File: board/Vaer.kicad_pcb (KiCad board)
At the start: 2 copper layers, 0 parts

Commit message: :sparkles: Add an initial outline for the board
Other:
- board outline added: 84.4 x 84.4 mm
- board text added: "${TITLE} Version ${REVISION} Design finished on ${ISSUE_DATE}"

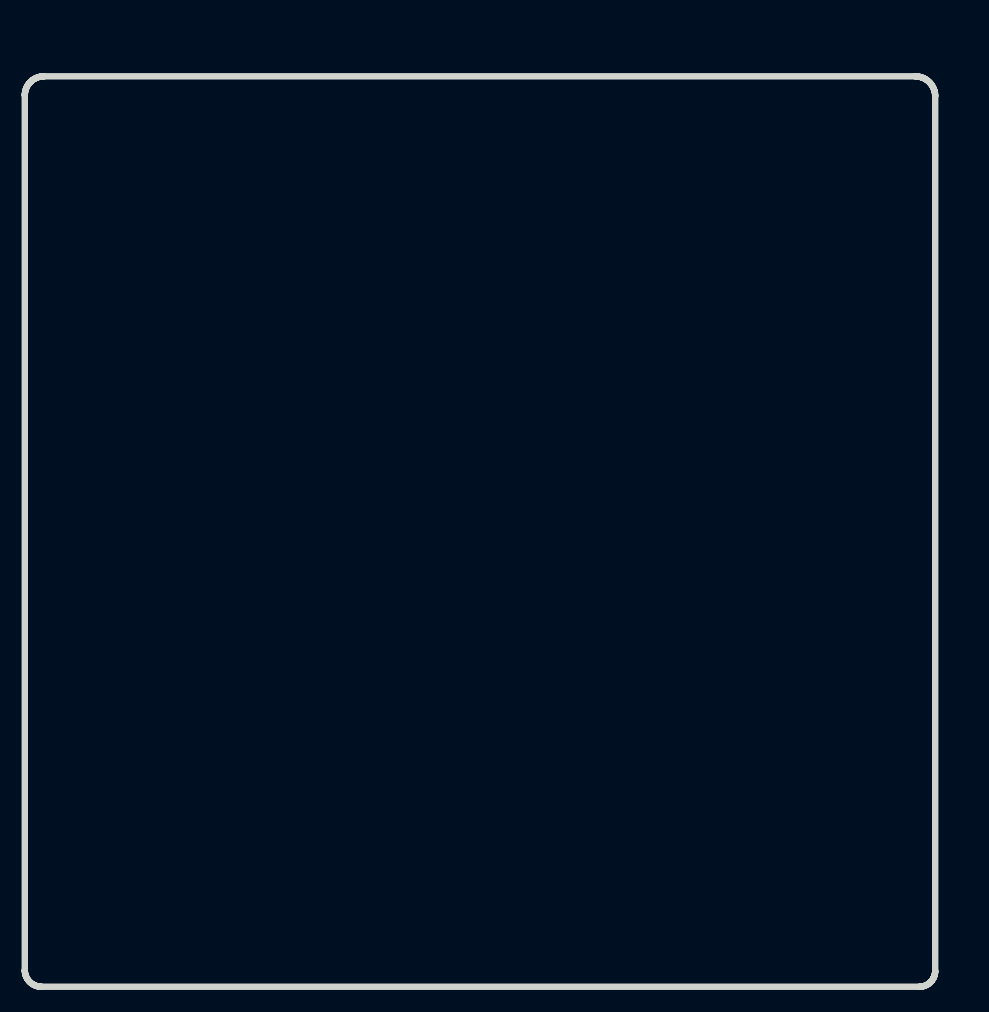
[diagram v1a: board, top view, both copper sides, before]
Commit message: :recycle: Add a notch for the PCB antenna of the MCU
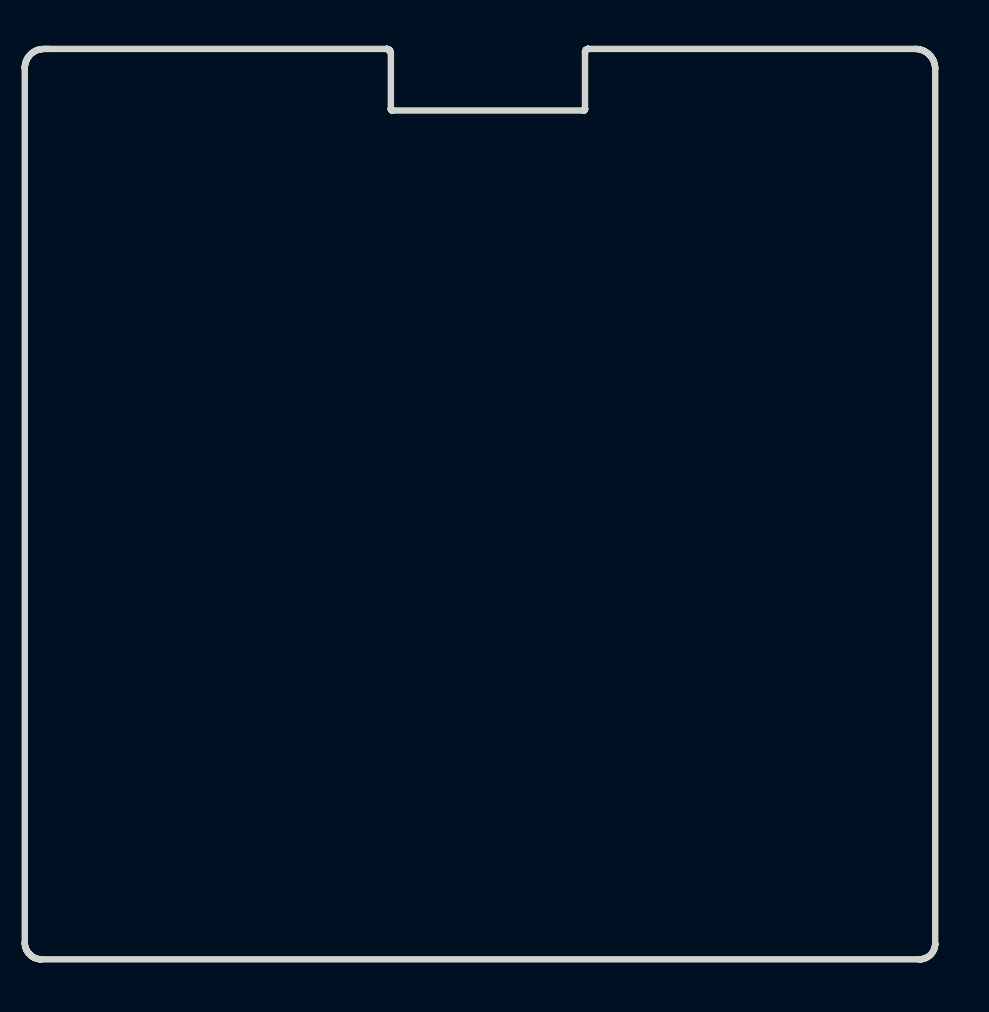
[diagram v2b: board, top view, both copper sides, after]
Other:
- outline, holes or cut-outs redrawn

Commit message: :construction: Start layouting the actual PCB
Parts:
- added BT1: Battery_Cell, Battery:BatteryHolder_MPD_BH-18650-PC2, F.Cu at (110.0, 111.8)
- added C1: 100nF, Capacitor_SMD:C_1206_3216Metric_Pad1.33x1.80mm_HandSolder, F.Cu at (110.4, 72.2)
- added C2: 100nF, Capacitor_SMD:C_1206_3216Metric_Pad1.33x1.80mm_HandSolder, F.Cu at (110.4, 77.3)
- added C3: 4.7uF, Capacitor_SMD:C_1206_3216Metric_Pad1.33x1.80mm_HandSolder, F.Cu at (133.0, 93.0)
- added C4: 10uF, Capacitor_SMD:C_1206_3216Metric_Pad1.33x1.80mm_HandSolder, F.Cu at (162.6, 86.4)
- added C5: 10uF, Capacitor_SMD:C_1206_3216Metric_Pad1.33x1.80mm_HandSolder, F.Cu at (167.6, 86.4)
- added C6: 1uF, Capacitor_SMD:C_1206_3216Metric_Pad1.33x1.80mm_HandSolder, F.Cu at (124.4, 93.0)
- added D1: LED_BLUE_PWR, LED_SMD:LED_1206_3216Metric_Pad1.42x1.75mm_HandSolder, F.Cu at (178.9, 76.2)
- added D2: LED_YELLOW, LED_SMD:LED_1206_3216Metric_Pad1.42x1.75mm_HandSolder, F.Cu at (178.9, 71.1)
- added D3: LED_GREEN, LED_SMD:LED_1206_3216Metric_Pad1.42x1.75mm_HandSolder, F.Cu at (178.9, 66.0)
- added H1: MountingHole_Pad, MountingHole:MountingHole_2.2mm_M2_Pad_Via, F.Cu at (108.0, 53.3)
- added H2: MountingHole_Pad, MountingHole:MountingHole_2.2mm_M2_Pad_Via, F.Cu at (184.5, 53.3)
- added H3: MountingHole_Pad, MountingHole:MountingHole_2.2mm_M2_Pad_Via, F.Cu at (108.0, 127.8)
- added H4: MountingHole_Pad, MountingHole:MountingHole_2.2mm_M2_Pad_Via, F.Cu at (184.5, 127.8)
- added J1: 105450-0101, Library:MOLEX_105450-0101, F.Cu at (138.5, 129.9)
- added R1: 5k1, Resistor_SMD:R_1206_3216Metric_Pad1.30x1.75mm_HandSolder, F.Cu at (152.5, 127.0)
- added R2: 5k1, Resistor_SMD:R_1206_3216Metric_Pad1.30x1.75mm_HandSolder, F.Cu at (152.5, 130.4)
- added R3: 120, Resistor_SMD:R_1206_3216Metric_Pad1.30x1.75mm_HandSolder, F.Cu at (168.8, 76.2)
- added R4: 1k5, Resistor_SMD:R_1206_3216Metric_Pad1.30x1.75mm_HandSolder, F.Cu at (168.8, 71.1)
- added R5: 1k5, Resistor_SMD:R_1206_3216Metric_Pad1.30x1.75mm_HandSolder, F.Cu at (168.8, 66.0)
- added R6: 10k, Resistor_SMD:R_1206_3216Metric_Pad1.30x1.75mm_HandSolder, F.Cu at (124.4, 97.1)
- added R7: 10k, Resistor_SMD:R_1206_3216Metric_Pad1.30x1.75mm_HandSolder, F.Cu at (142.2, 86.4)
- added R8: 1k18, Resistor_SMD:R_1206_3216Metric_Pad1.30x1.75mm_HandSolder, F.Cu at (147.3, 86.4)
- added R9: 1k13, Resistor_SMD:R_1206_3216Metric_Pad1.30x1.75mm_HandSolder, F.Cu at (152.4, 86.4)
- added SW_FLASH1: Flash mode, Button_Switch_THT:SW_PUSH_6mm, F.Cu at (177.1, 93.0)
- added SW_RESET1: Reset, Button_Switch_THT:SW_PUSH_6mm, F.Cu at (108.5, 93.0)
- added TP1: TestPoint, TestPoint:TestPoint_Pad_D1.0mm, F.Cu at (177.1, 88.9)
- added TP2: TestPoint, TestPoint:TestPoint_Pad_D1.0mm, F.Cu at (108.5, 88.9)
- added U2: NCP1117-3.3_SOT223, Package_TO_SOT_SMD:SOT-223-3_TabPin2, F.Cu at (165.1, 95.2)
- added U3: BQ24073RGT, Package_DFN_QFN:VQFN-16-1EP_3x3mm_P0.5mm_EP1.6x1.6mm, F.Cu at (146.6, 94.8)
- added U4: BME280, Package_LGA:Bosch_LGA-8_2.5x2.5mm_P0.65mm_ClockwisePinNumbering, F.Cu at (117.1, 74.7)
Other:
- board text added: "Humidity Pressure Temperature"
- board text added: "PWR"
- board text added: "TP EN"
- board text added: "TP PROG"
- board text added: "locked"
- board text added: "~{CHG}"
- board text added: "~{PGOOD}"
- board text removed: "${TITLE} Version ${REVISION} Design finished on ${ISSUE_DATE}"

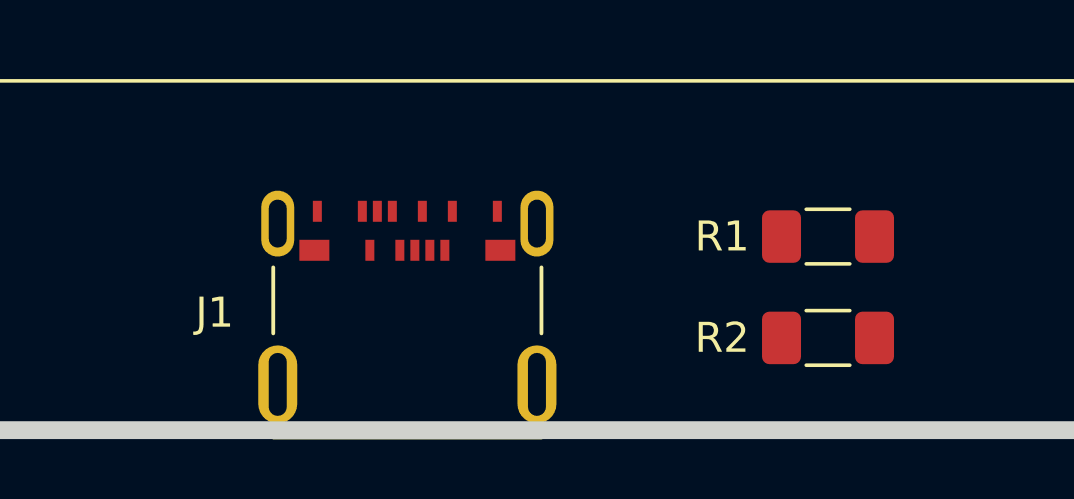
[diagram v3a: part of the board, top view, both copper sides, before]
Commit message: :fire: Remove dysfunctional libraries
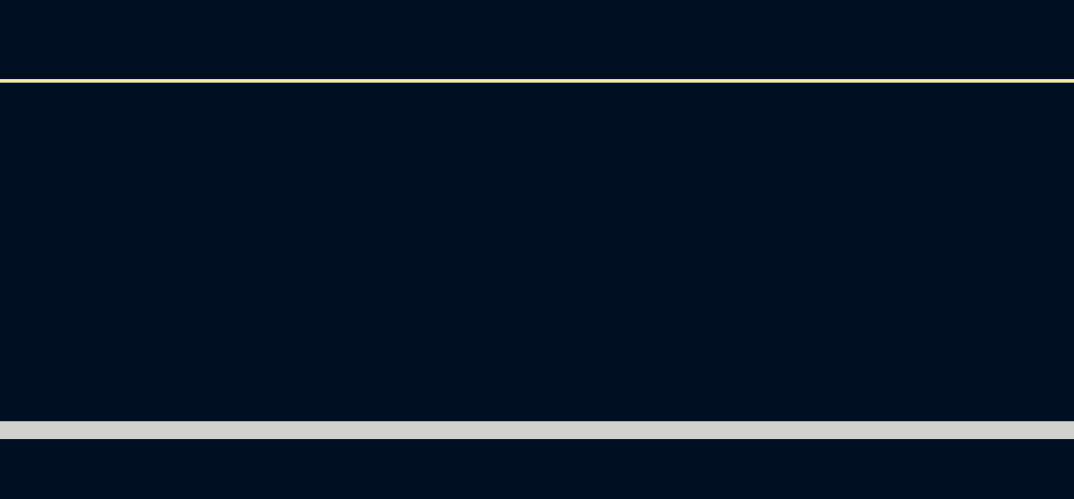
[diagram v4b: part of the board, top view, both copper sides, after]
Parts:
- removed J1: 105450-0101, Library:MOLEX_105450-0101
- removed R1, R2: 5k1, Resistor_SMD:R_1206_3216Metric_Pad1.30x1.75mm_HandSolder

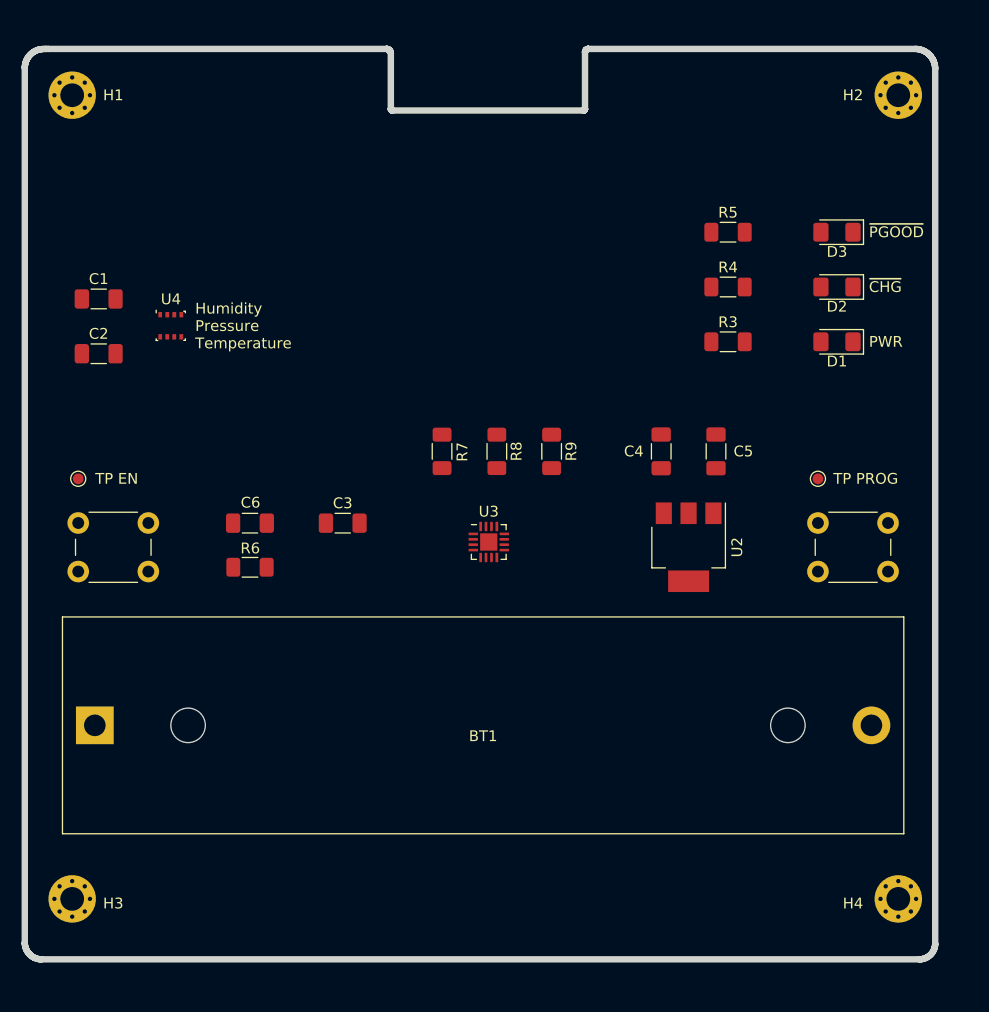
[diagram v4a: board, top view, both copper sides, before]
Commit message: :sparkles: Place all components onto the board
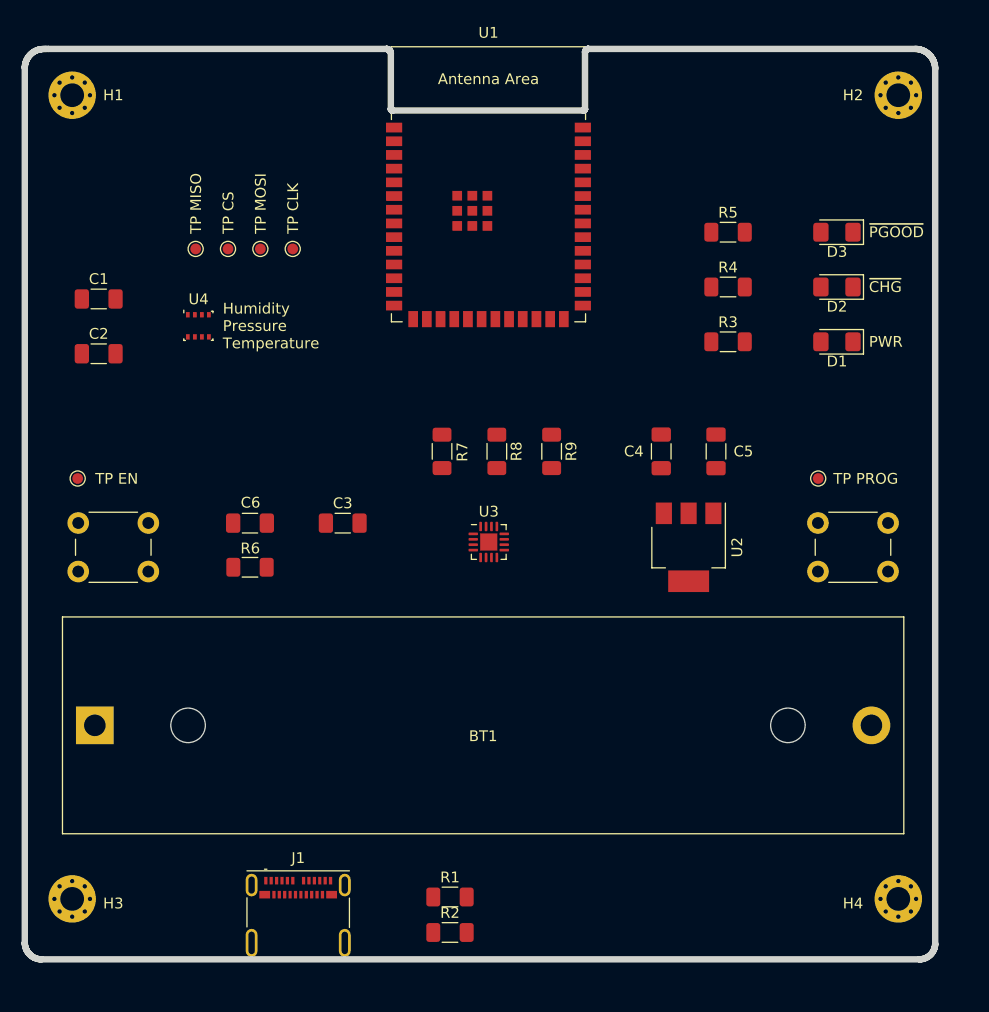
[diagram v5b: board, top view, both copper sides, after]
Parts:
- added J1: USB_C_Receptacle, Connector_USB:USB_C_Receptacle_Molex_105450-0101, F.Cu at (128.9, 129.4)
- added R1: 5k1, Resistor_SMD:R_1206_3216Metric_Pad1.30x1.75mm_HandSolder, F.Cu at (143.0, 127.7)
- added R2: 5k1, Resistor_SMD:R_1206_3216Metric_Pad1.30x1.75mm_HandSolder, F.Cu at (143.0, 131.0)
- added TP3: TestPoint, TestPoint:TestPoint_Pad_D1.0mm, F.Cu at (125.4, 67.6)
- added TP4: TestPoint, TestPoint:TestPoint_Pad_D1.0mm, F.Cu at (128.4, 67.6)
- added TP5: TestPoint, TestPoint:TestPoint_Pad_D1.0mm, F.Cu at (177.1, 88.9)
- added TP6: TestPoint, TestPoint:TestPoint_Pad_D1.0mm, F.Cu at (108.5, 88.9)
- added U1: ESP32-S3-WROOM-1, Espressif:ESP32-S3-WROOM-1, F.Cu at (146.5, 64.6)
- moved TP1 61.5 mm to (119.4, 67.6)
- moved TP2 25.4 mm to (122.4, 67.6)
- moved U4 2.56 mm to (119.6, 74.7)
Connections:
- TP1 pad 1: PROG -> MISO
- TP2 pad 1: EN -> CS
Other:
- board text added: "TP CLK"
- board text added: "TP CS"
- board text added: "TP MISO"
- board text added: "TP MOSI"

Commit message: :construction: Start wiring all components
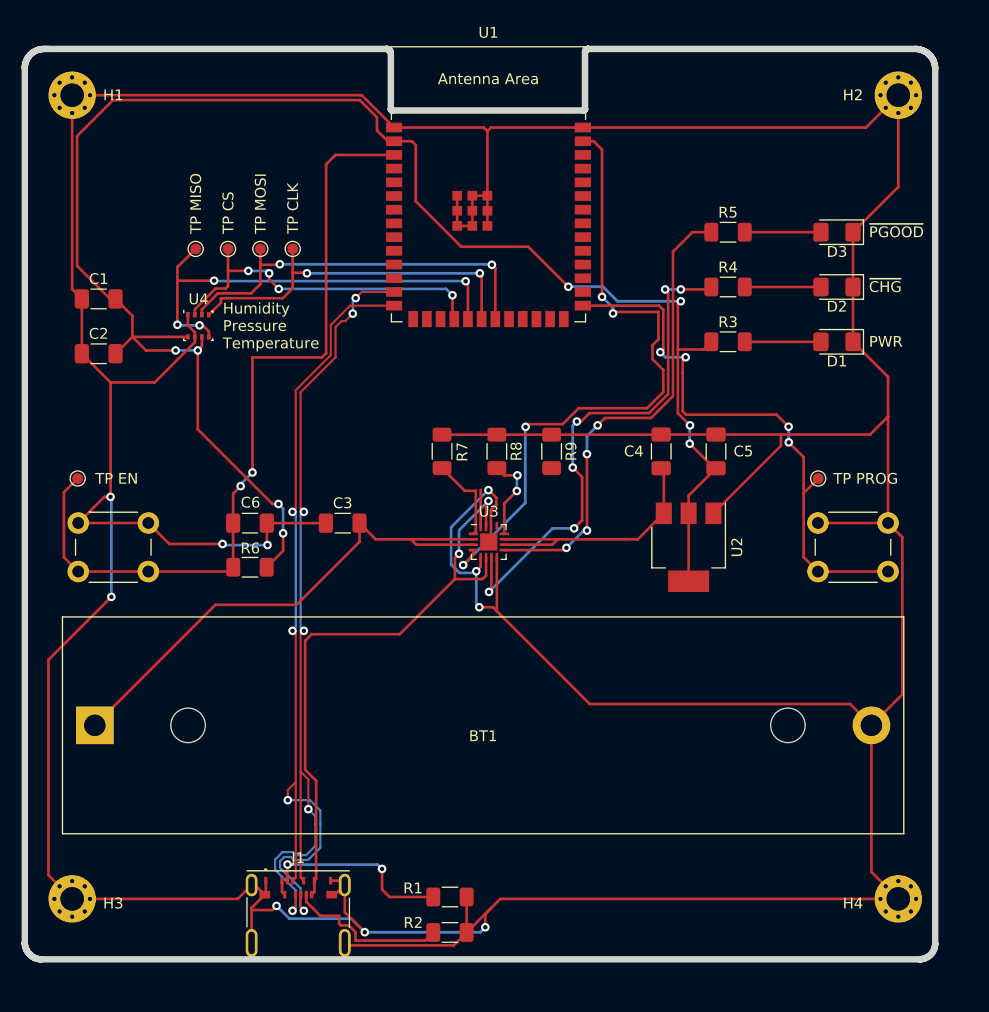
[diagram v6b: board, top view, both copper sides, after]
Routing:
- net GND: track 0.00 -> 538.7 mm, vias 0 -> 10
- net VCC_ESP: track 0.00 -> 161.7 mm, vias 0 -> 8
- net D+: track 0.00 -> 80.6 mm, vias 0 -> 4
- net D-: track 0.00 -> 80.0 mm, vias 0 -> 6
- net EN: track 0.00 -> 75.6 mm, vias 0 -> 2
- net ~{CE}: track 0.00 -> 61.1 mm, vias 0 -> 4
- net VCC_EBUS: track 0.00 -> 57.5 mm, vias 0 -> 2
- net PROG: track 0.00 -> 52.7 mm, vias 0 -> 4
- net Net-(BT1-+): track 0.00 -> 50.5 mm
- net ~{CHG}: track 0.00 -> 48.0 mm, vias 0 -> 6
- net ~{PGOOD}: track 0.00 -> 44.4 mm, vias 0 -> 4
- net MISO: track 0.00 -> 41.8 mm, vias 0 -> 4
- net MOSI: track 0.00 -> 36.8 mm, vias 0 -> 2
- net SCLK: track 0.00 -> 34.4 mm, vias 0 -> 2
- net CS: track 0.00 -> 32.3 mm, vias 0 -> 4
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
